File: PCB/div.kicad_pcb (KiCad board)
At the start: 2 copper layers, 31.5 x 110.5 mm, 63 parts, among them J1 Rst, J10 OUT, J2 Bus Gate Reset, J3 Clk, J4 PWR, J5 OUT, J6 OUT, J7 OUT, J8 OUT, J9 OUT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

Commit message: :sparkles: Add SMD LEDs to PCB
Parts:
- added D13: gn, LED_SMD:LED_0805_2012Metric_Pad1.15x1.40mm_HandSolder, F.Cu at (117.8, 78.1)
- added D14: gn, LED_SMD:LED_0805_2012Metric_Pad1.15x1.40mm_HandSolder, F.Cu at (117.8, 92.2)
- added D15: gn, LED_SMD:LED_0805_2012Metric_Pad1.15x1.40mm_HandSolder, F.Cu at (117.8, 106.3)
- added D16: gn, LED_SMD:LED_0805_2012Metric_Pad1.15x1.40mm_HandSolder, F.Cu at (117.8, 120.4)
- added D17: gn, LED_SMD:LED_0805_2012Metric_Pad1.15x1.40mm_HandSolder, F.Cu at (117.8, 134.4)
- added D18: gn, LED_SMD:LED_0805_2012Metric_Pad1.15x1.40mm_HandSolder, F.Cu at (117.8, 148.5)
- added D19: gn, LED_SMD:LED_0805_2012Metric_Pad1.15x1.40mm_HandSolder, F.Cu at (117.8, 50.0)
- added D20: gn, LED_SMD:LED_0805_2012Metric_Pad1.15x1.40mm_HandSolder, F.Cu at (117.8, 64.1)
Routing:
- net Net-(D12-K): track 10.1 -> 22.1 mm
- net Net-(D10-A): track 12.7 -> 24.4 mm
- net Net-(D15-A): track 12.6 -> 24.3 mm
- net Net-(D14-A): track 12.6 -> 24.3 mm
- net Net-(D13-A): track 12.6 -> 24.3 mm
- net Net-(D11-A): track 12.6 -> 24.2 mm
- net /RESET_IN: track 40.0 -> 51.6 mm
- net +12V: track 140.2 -> 151.7 mm
- net Net-(D12-A): track 9.54 -> 20.9 mm
- net Net-(D20-K): track 3.16 -> 12.9 mm
- net Net-(D11-K): track 3.16 -> 12.9 mm
- net Net-(D13-K): track 3.19 -> 12.9 mm
- net Net-(D14-K): track 3.21 -> 12.9 mm
- net Net-(D15-K): track 3.24 -> 12.9 mm
- net Net-(D10-K): track 3.27 -> 12.9 mm
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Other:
- board text added: "Populate either SMD or THT LED"

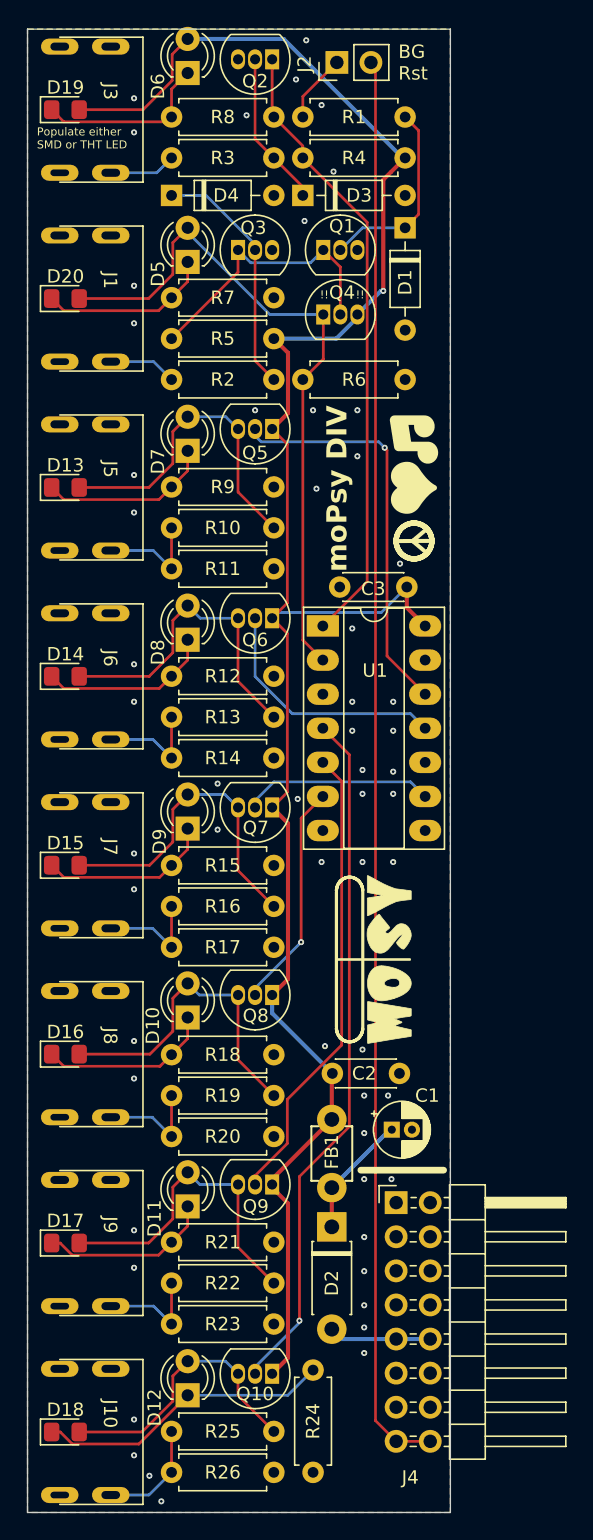
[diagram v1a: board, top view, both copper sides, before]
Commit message: :hammer: Adapt PCB to vertical header and turn red stripe down
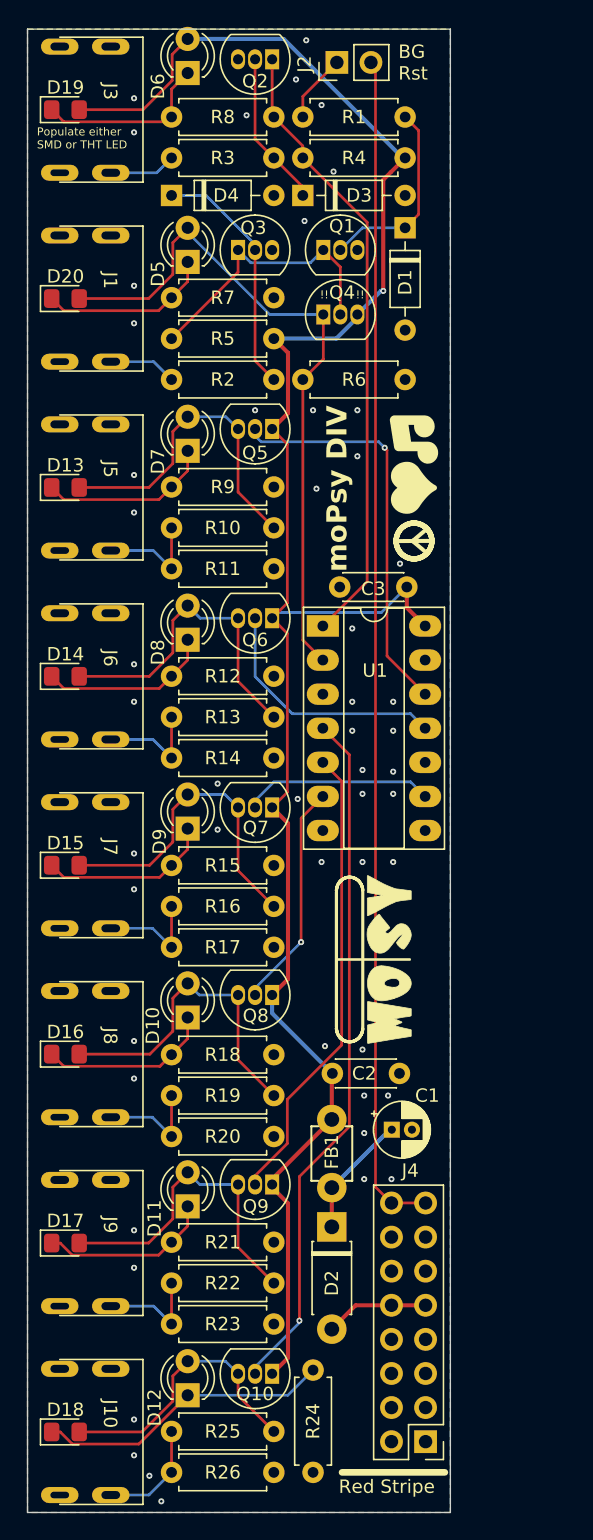
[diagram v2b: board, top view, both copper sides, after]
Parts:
- J4: footprint Connector_PinHeader_2.54mm:PinHeader_2x08_P2.54mm_Horizontal -> Connector_PinHeader_2.54mm:PinHeader_2x08_P2.54mm_Vertical
- moved J4 17.9 mm to (144.7, 149.2), turned to 180 degrees
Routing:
- net Gate: track 106.0 -> 88.1 mm
- net GND: vias 57 -> 52

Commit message: :art: Leave more room around the power connector
This is needed for the box header.
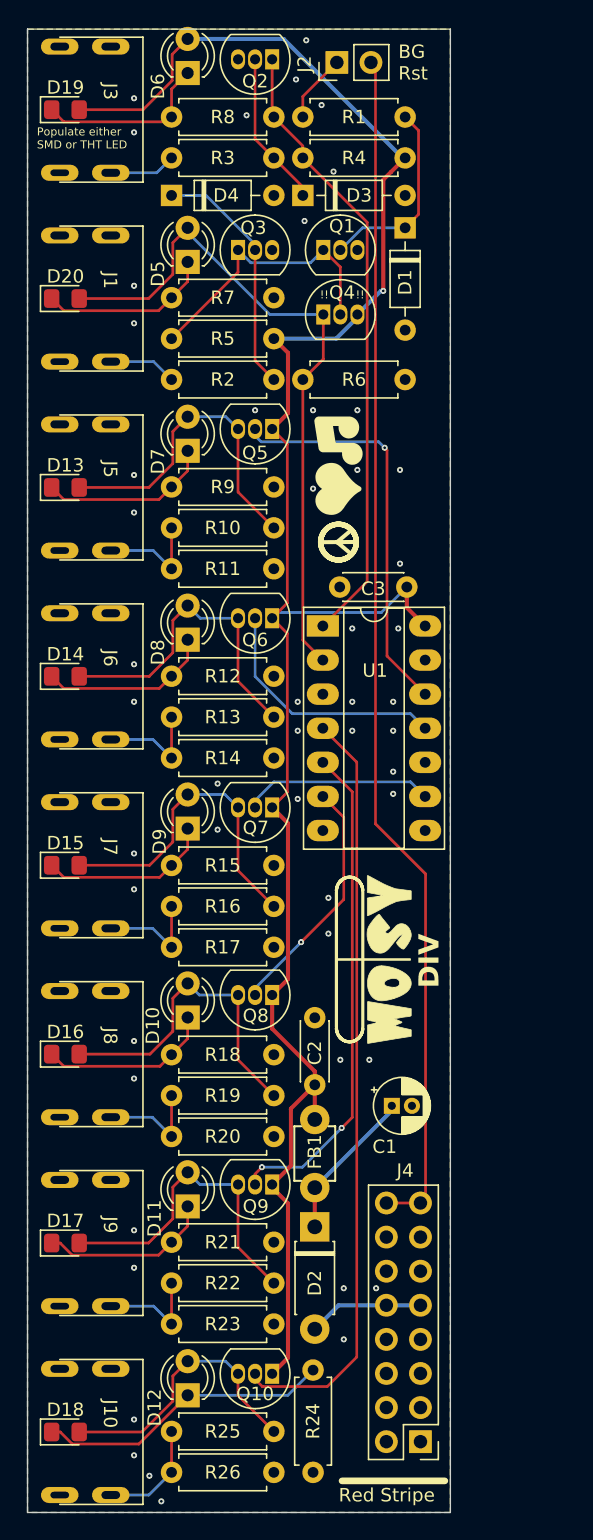
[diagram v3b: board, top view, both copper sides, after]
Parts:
- moved C1 1.78 mm to (142.1, 124.2)
- moved C2 1.56 mm to (136.4, 122.6), turned to 90 degrees
- moved D2 1.27 mm to (136.4, 133.2)
- moved FB1 1.27 mm to (136.4, 127.8)
- moved J4 0.38 mm to (144.3, 149.2)
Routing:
- net /Gate Output 64/GATE_OUT: track 51.8 -> 57.0 mm, vias 1 -> 0
- net Net-(D2-K): track 9.18 -> 11.8 mm
- net /Gate Output 32/GATE_OUT: track 34.7 -> 37.1 mm, vias 0 -> 2
- net +12V: track 151.7 -> 153.1 mm
- net /Gate Output 16/GATE_OUT: track 16.9 -> 18.2 mm
- net Gate: track 88.1 -> 89.3 mm
- net Net-(D2-A): track 7.72 -> 8.61 mm
- net GND: vias 52 -> 51
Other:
- board text added: "DIV"
- board text removed: "moPsy DIV"

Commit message: :bento: Update PCB to set correct resistor values
In #20 the resistor values have been changed in the schematic.

As this was no PCB change, I did not mind to update the PCB file. However,
the old resistor values are now shown there and also in the BOM.

This is only an update to the resistor values stored in the PCB file, no changes
to the actual PCB layout have been made.
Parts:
- R1, R2, R3: value 10k -> 100k
- R10, R11, R13, R14, R16, R17, R19, R20, R22, R23, R25, R26: value 4k7 -> 2k2
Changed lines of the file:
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@@
         (effects (font (size 1 1) (thickness 0.15)))
     )
-    (fp_text value "4k7" (at 3.81 2.37) (layer "F.Fab")
+    (fp_text value "2k2" (at 3.81 2.37) (layer "F.Fab")
         (effects (font (size 1 1) (thickness 0.15)))
     )
@@
         (effects (font (size 1 1) (thickness 0.15)))
     )
-    (fp_text value "4k7" (at 3.81 2.37) (layer "F.Fab")
+    (fp_text value "2k2" (at 3.81 2.37) (layer "F.Fab")
         (effects (font (size 1 1) (thickness 0.15)))
     )
@@
         (effects (font (size 1 1) (thickness 0.15)))
     )
-    (fp_text value "4k7" (at 3.81 2.37) (layer "F.Fab")
+    (fp_text value "2k2" (at 3.81 2.37) (layer "F.Fab")
         (effects (font (size 1 1) (thickness 0.15)))
     )
@@
         (effects (font (size 1 1) (thickness 0.15)))
     )
-    (fp_text value "10k" (at 3.81 2.37) (layer "F.Fab")
+    (fp_text value "100k" (at 3.81 2.37) (layer "F.Fab")
         (effects (font (size 1 1) (thickness 0.15)))
     )
@@
         (effects (font (size 1 1) (thickness 0.15)))
     )
-    (fp_text value "10k" (at 3.81 2.37) (layer "F.Fab")
+    (fp_text value "100k" (at 3.81 2.37) (layer "F.Fab")
         (effects (font (size 1 1) (thickness 0.15)))
     )
@@
         (effects (font (size 1 1) (thickness 0.15)))
     )
-    (fp_text value "4k7" (at 3.81 2.37) (layer "F.Fab")
+    (fp_text value "2k2" (at 3.81 2.37) (layer "F.Fab")
         (effects (font (size 1 1) (thickness 0.15)))
     )
@@
         (effects (font (size 1 1) (thickness 0.15)))
     )
-    (fp_text value "4k7" (at 3.81 2.37) (layer "F.Fab")
+    (fp_text value "2k2" (at 3.81 2.37) (layer "F.Fab")
         (effects (font (size 1 1) (thickness 0.15)))
     )
@@
         (effects (font (size 1 1) (thickness 0.15)))
     )
-    (fp_text value "4k7" (at 3.81 2.37) (layer "F.Fab")
+    (fp_text value "2k2" (at 3.81 2.37) (layer "F.Fab")
         (effects (font (size 1 1) (thickness 0.15)))
     )
@@
         (effects (font (size 1 1) (thickness 0.15)))
     )
-    (fp_text value "4k7" (at 3.81 2.37) (layer "F.Fab")
+    (fp_text value "2k2" (at 3.81 2.37) (layer "F.Fab")
         (effects (font (size 1 1) (thickness 0.15)))
     )
@@
         (effects (font (size 1 1) (thickness 0.15)))
     )
-    (fp_text value "4k7" (at 3.81 2.37) (layer "F.Fab")
+    (fp_text value "2k2" (at 3.81 2.37) (layer "F.Fab")
         (effects (font (size 1 1) (thickness 0.15)))
     )
@@
         (effects (font (size 1 1) (thickness 0.15)))
     )
-    (fp_text value "10k" (at 3.81 2.37) (layer "F.Fab")
+    (fp_text value "100k" (at 3.81 2.37) (layer "F.Fab")
         (effects (font (size 1 1) (thickness 0.15)))
     )
@@
         (effects (font (size 1 1) (thickness 0.15)))
     )
-    (fp_text value "4k7" (at 3.81 2.37) (layer "F.Fab")
+    (fp_text value "2k2" (at 3.81 2.37) (layer "F.Fab")
         (effects (font (size 1 1) (thickness 0.15)))
     )
@@
         (effects (font (size 1 1) (thickness 0.15)))
     )
-    (fp_text value "4k7" (at 3.81 2.37) (layer "F.Fab")
+    (fp_text value "2k2" (at 3.81 2.37) (layer "F.Fab")
         (effects (font (size 1 1) (thickness 0.15)))
     )
@@
         (effects (font (size 1 1) (thickness 0.15)))
     )
-    (fp_text value "4k7" (at 3.81 2.37) (layer "F.Fab")
+    (fp_text value "2k2" (at 3.81 2.37) (layer "F.Fab")
         (effects (font (size 1 1) (thickness 0.15)))
     )
@@
         (effects (font (size 1 1) (thickness 0.15)))
     )
-    (fp_text value "4k7" (at 3.81 2.37) (layer "F.Fab")
+    (fp_text value "2k2" (at 3.81 2.37) (layer "F.Fab")
         (effects (font (size 1 1) (thickness 0.15)))
     )

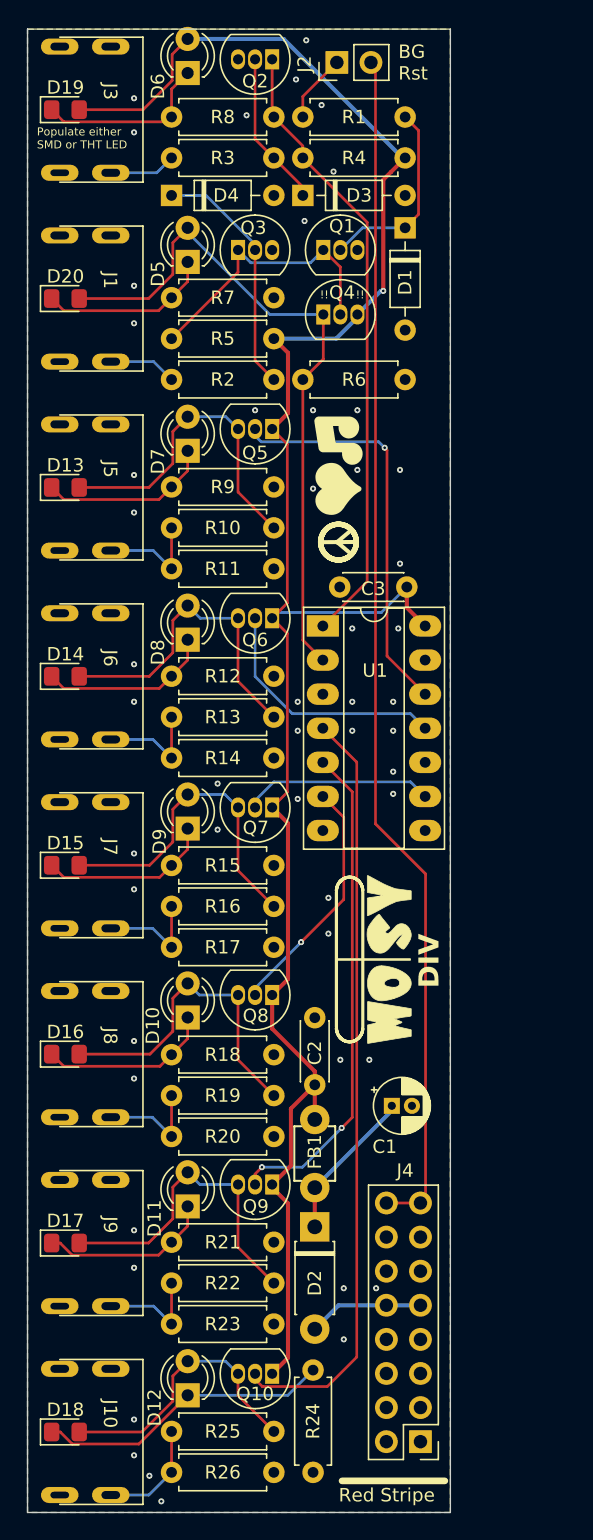
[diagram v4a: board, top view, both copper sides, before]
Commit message: :wrench: Adjust PCB to changed transistor footprint
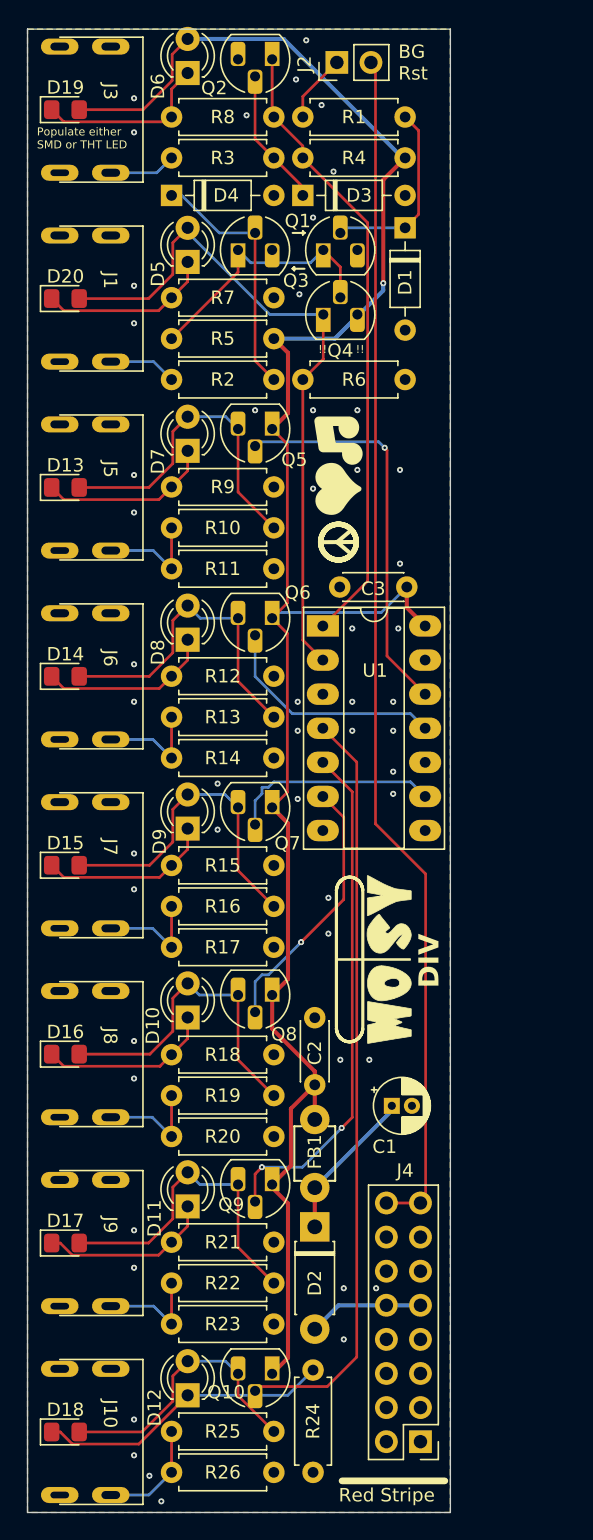
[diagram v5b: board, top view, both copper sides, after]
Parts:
- Q1, Q10, Q2, Q3, Q4, Q5, Q6, Q7, Q8, Q9: footprint Package_TO_SOT_THT:TO-92_Inline -> Package_TO_SOT_THT:TO-92_HandSolder
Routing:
- net /Gate Output 8/GATE_OUT: track 14.2 -> 15.8 mm
- net /Gate Output 16/GATE_OUT: track 18.2 -> 19.7 mm
- net /Gate Output 32/GATE_OUT: track 37.1 -> 38.4 mm
- net Net-(Q1-C): track 21.1 -> 19.9 mm
- net Net-(D3-K): track 11.6 -> 10.3 mm
- net /Gate Output 4/GATE_OUT: track 18.6 -> 17.3 mm
- net /Gate Output 2/GATE_OUT: track 30.1 -> 29.6 mm
- net Net-(D1-K): track 14.6 -> 14.1 mm
- net /Gate Output 64/GATE_OUT: track 57.0 -> 56.5 mm
- net Net-(D4-K): track 18.4 -> 18.9 mm
- net GND: vias 51 -> 52

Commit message: :sparkles: Add an LED bending gauge
Allows to bend the LEDs exactly while building the module.
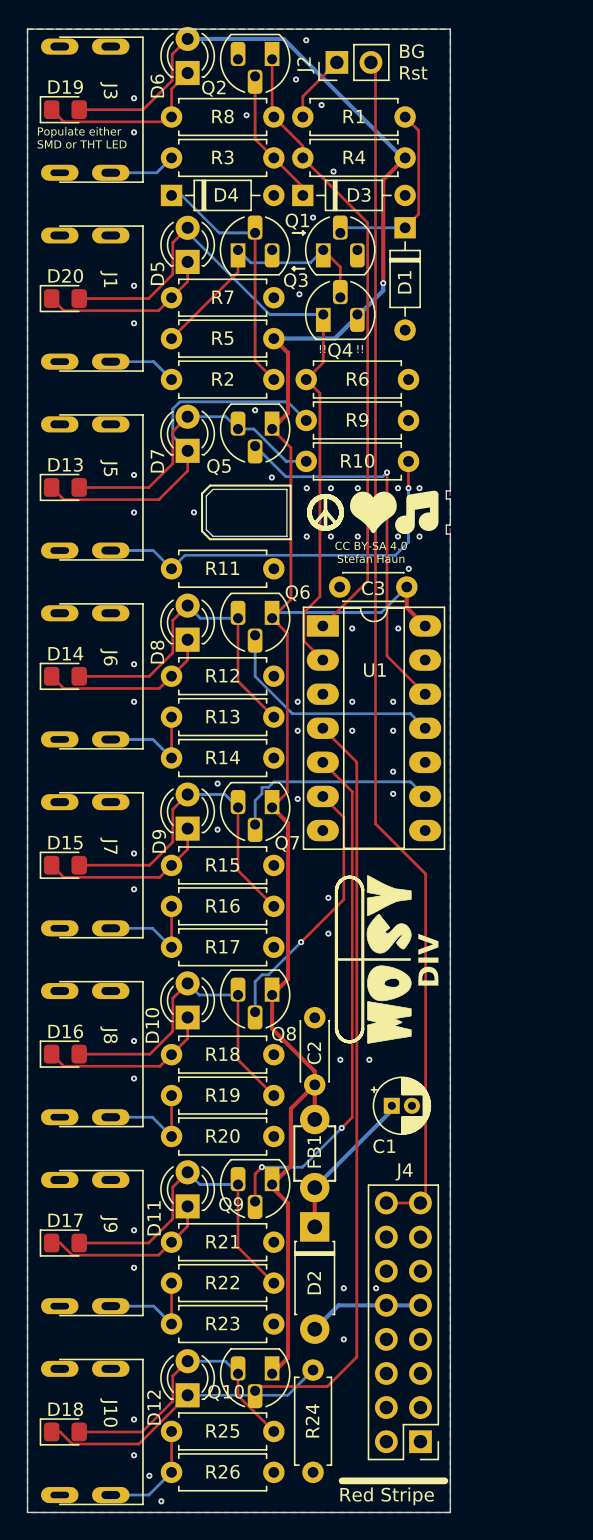
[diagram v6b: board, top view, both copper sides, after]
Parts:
- moved R10 18.3 mm to (143.4, 76.2), turned to 180 degrees
- moved R9 11.2 mm to (143.4, 73.2)
- moved R6 0.25 mm to (143.4, 70.1)
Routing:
- net Net-(J5-PadT): track 8.14 -> 29.6 mm, vias 0 -> 1
- net Net-(D13-K): track 12.9 -> 27.2 mm
- net Net-(D13-A): track 24.3 -> 21.9 mm
- net /Gate Output 2/GATE_OUT: track 29.6 -> 28.6 mm
- net /RESET_IN: track 51.6 -> 52.4 mm
- net GND: vias 52 -> 59
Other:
- outline, holes or cut-outs redrawn
- board text added: "A"
- board text added: "Bend LEDs here"
- board text added: "K"
